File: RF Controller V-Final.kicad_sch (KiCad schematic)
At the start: 36 parts, among them J2 J_OLED, J3 BAT+, J4 BAT-, SW1 EG1218, U1 Teensy4.0, U3 NRF24L01, U5 AP2112K-3.3, U7 Pitch/Roll, U8 TPS542025DDCR, U9 Throttle/Yaw

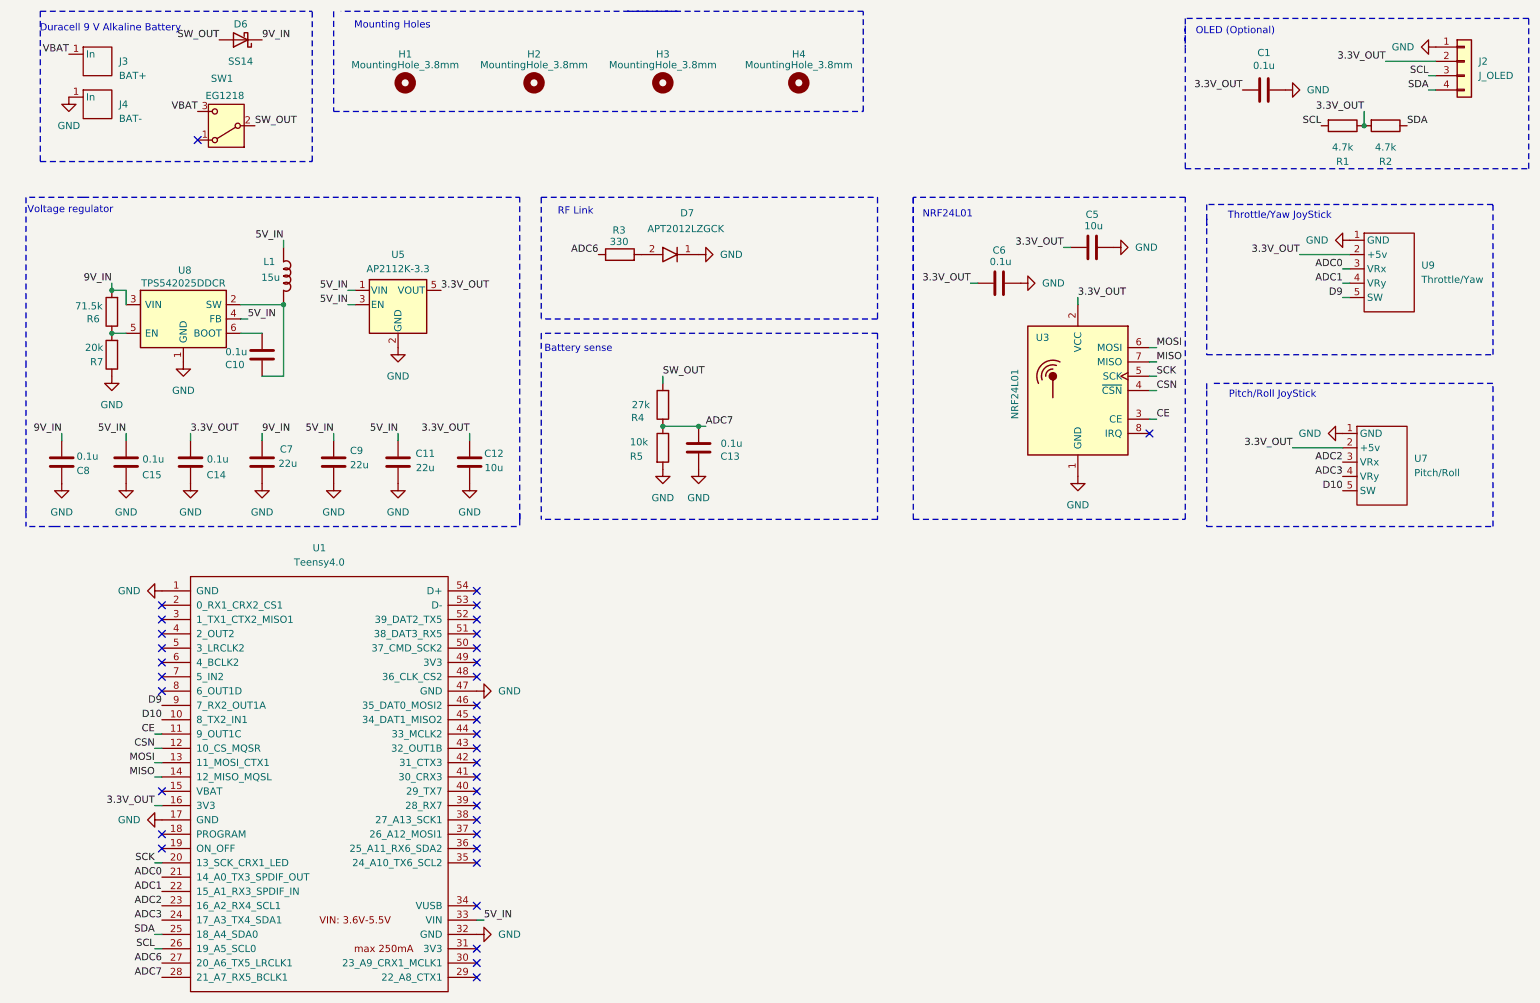
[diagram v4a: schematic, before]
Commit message: Added electrolytic cap
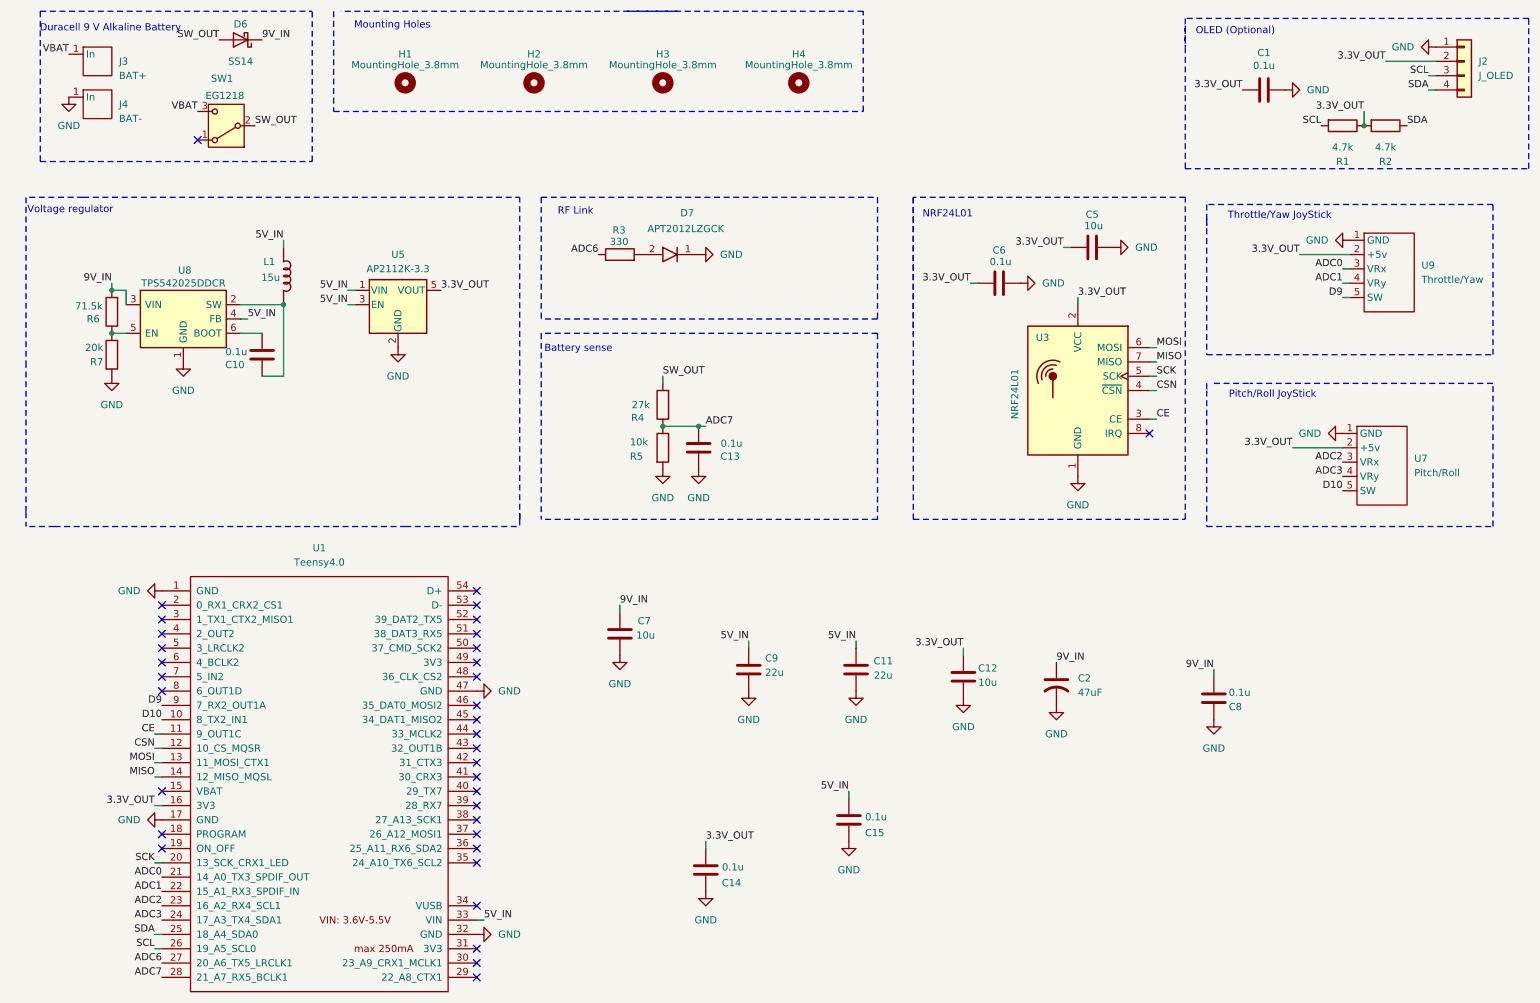
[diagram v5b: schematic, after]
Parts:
- added C2: 47uF, 865080543009:WCAP-ASLI_6.3X5.5_DXL_, symbol Device:C_US
- C7: value 22u -> 10u
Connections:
- net 9V_IN: now also C2.1
- net GND: now also C2.2
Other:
- moved on the sheet: C11, C12, C14, C15, C7, C8, C9
